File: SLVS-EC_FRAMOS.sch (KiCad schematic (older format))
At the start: 10 parts, among them J21 DF40HC(4.0)-60DS-0.4V(51)

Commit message: Pre-Production Push
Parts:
- added R45, R46: 1K, Resistor_SMD:R_0402_1005Metric, symbol Device:R
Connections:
- net DATA_4_N is gone; now on net SLVS_D1_N: J21.47 (Pin_47)
- net DATA_4_P is gone; now on net SLVS_D1_P: J21.45 (Pin_45)
- net DATA_6_N is gone; now on net SLVS_D0_N: J21.41 (Pin_41)
- net DATA_6_P is gone; now on net SLVS_D0_P: J21.39 (Pin_39)
- net HPC09_P_I2C_SLVS_EC_SCL: now also R46.1
- net HPC12_N_I2C_SLVS_EC_SDA: now also R45.1
- net PL_1V8: now also R45.2, R46.2
- net SLVS_D0_N: now also C261.2; no longer C259.1, J21.59 (Pin_59)
- net SLVS_D0_P: now also C262.2; no longer C260.1, J21.57 (Pin_57)
- net SLVS_D1_N: now also C259.1; no longer C261.2, J21.54 (Pin_54)
- net SLVS_D1_P: now also C260.1; no longer C262.2, J21.52 (Pin_52)
- net GTH_DP0_C2M_SLVS_EC_RX_N renamed GTH_DP1_C2M_SLVS_EC_RX_LANE1_N
- net GTH_DP0_C2M_SLVS_EC_RX_P renamed GTH_DP1_C2M_SLVS_EC_RX_LANE1_P
- net GTH_DP1_C2M_SLVS_EC_RX_N renamed GTH_DP3_C2M_SLVS_EC_RX_LANE0_N
- net GTH_DP1_C2M_SLVS_EC_RX_P renamed GTH_DP3_C2M_SLVS_EC_RX_LANE0_P
- net HPC01_N_GPIO0(XMASTER) renamed HPC01_N_XMASTER
- net HPC06_P_MCLK_0_SLVS renamed HPC10_CC_P_MCLK_0_SLVS
- net HPC10_CC_P_GPIO16_SLAMODE1 renamed HPC_06_P_GPIO16_SLAMODE1
- new net DATA_0_N: J21.59 (Pin_59)
- new net DATA_0_P: J21.57 (Pin_57)
- new net DATA_1_N: J21.54 (Pin_54)
- new net DATA_1_P: J21.52 (Pin_52)
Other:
- note added: "Edit -> Have SCK and XCE and SDA pulled to PL 1V8\nto allow for I2C or SPI communication\nPull down MISO so it does not float"
- note added: "Note, FRAMOS's DATA_#_P/N \nis in respect to SLVS, not SLVS-EC.\nRemember to reference datasheet\n for SLVS-EC pinout"
- moved on the sheet: C254, C255, C256, C257, C259, C260, C261, C262, J21, R217

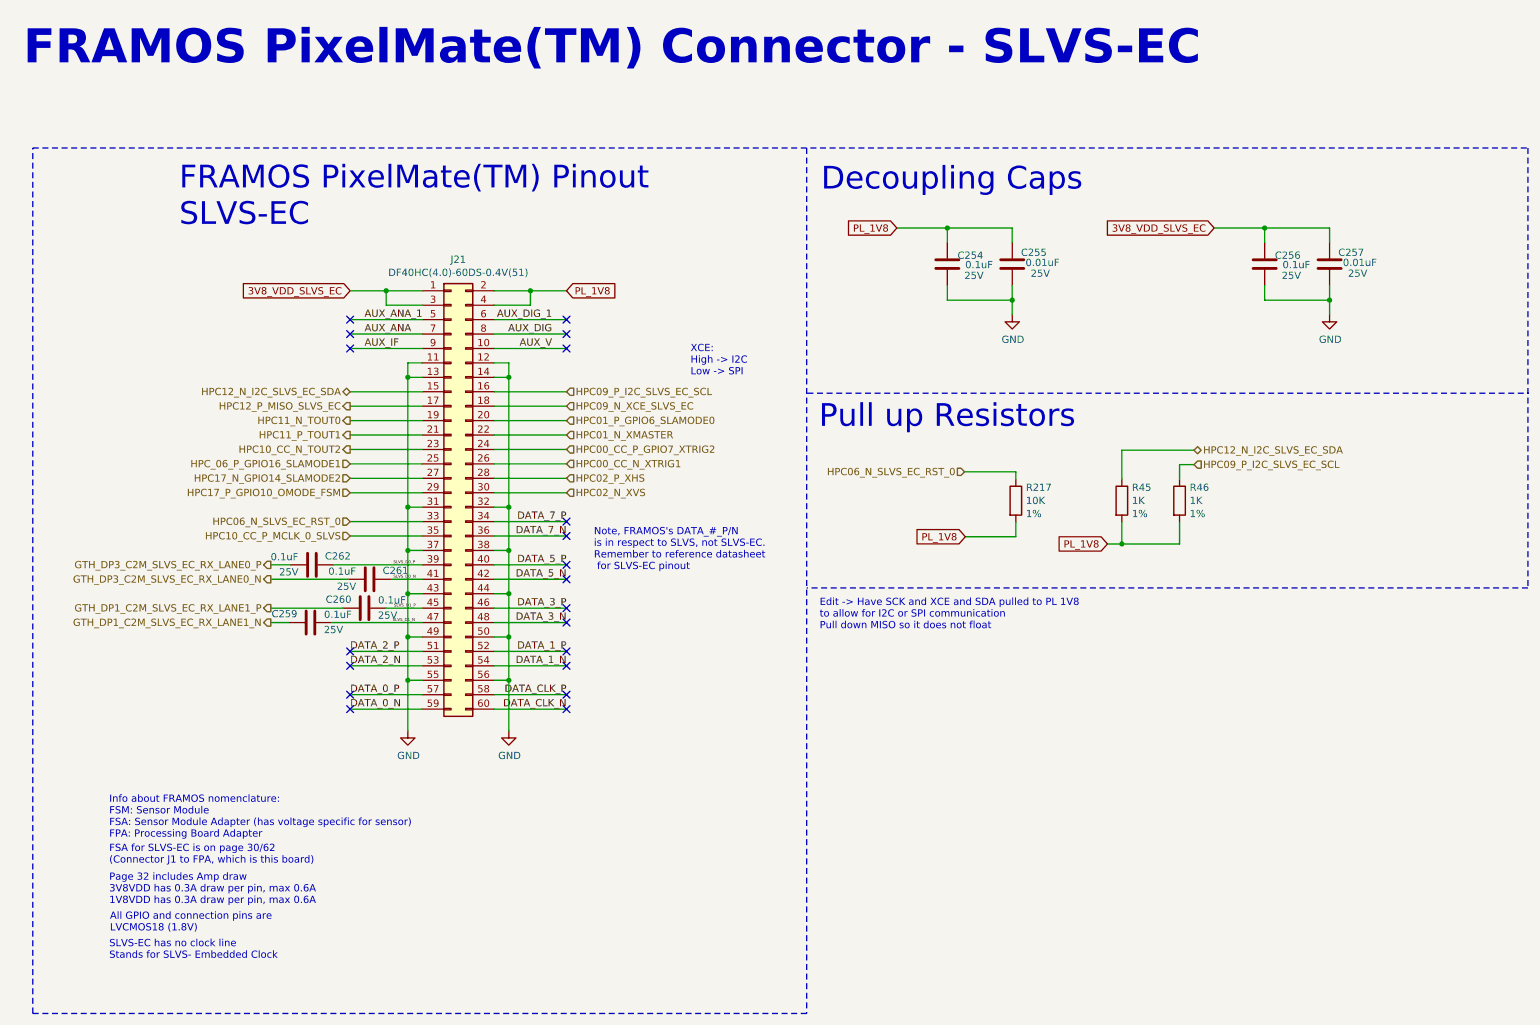
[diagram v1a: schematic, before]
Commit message: Update to Kicad 7
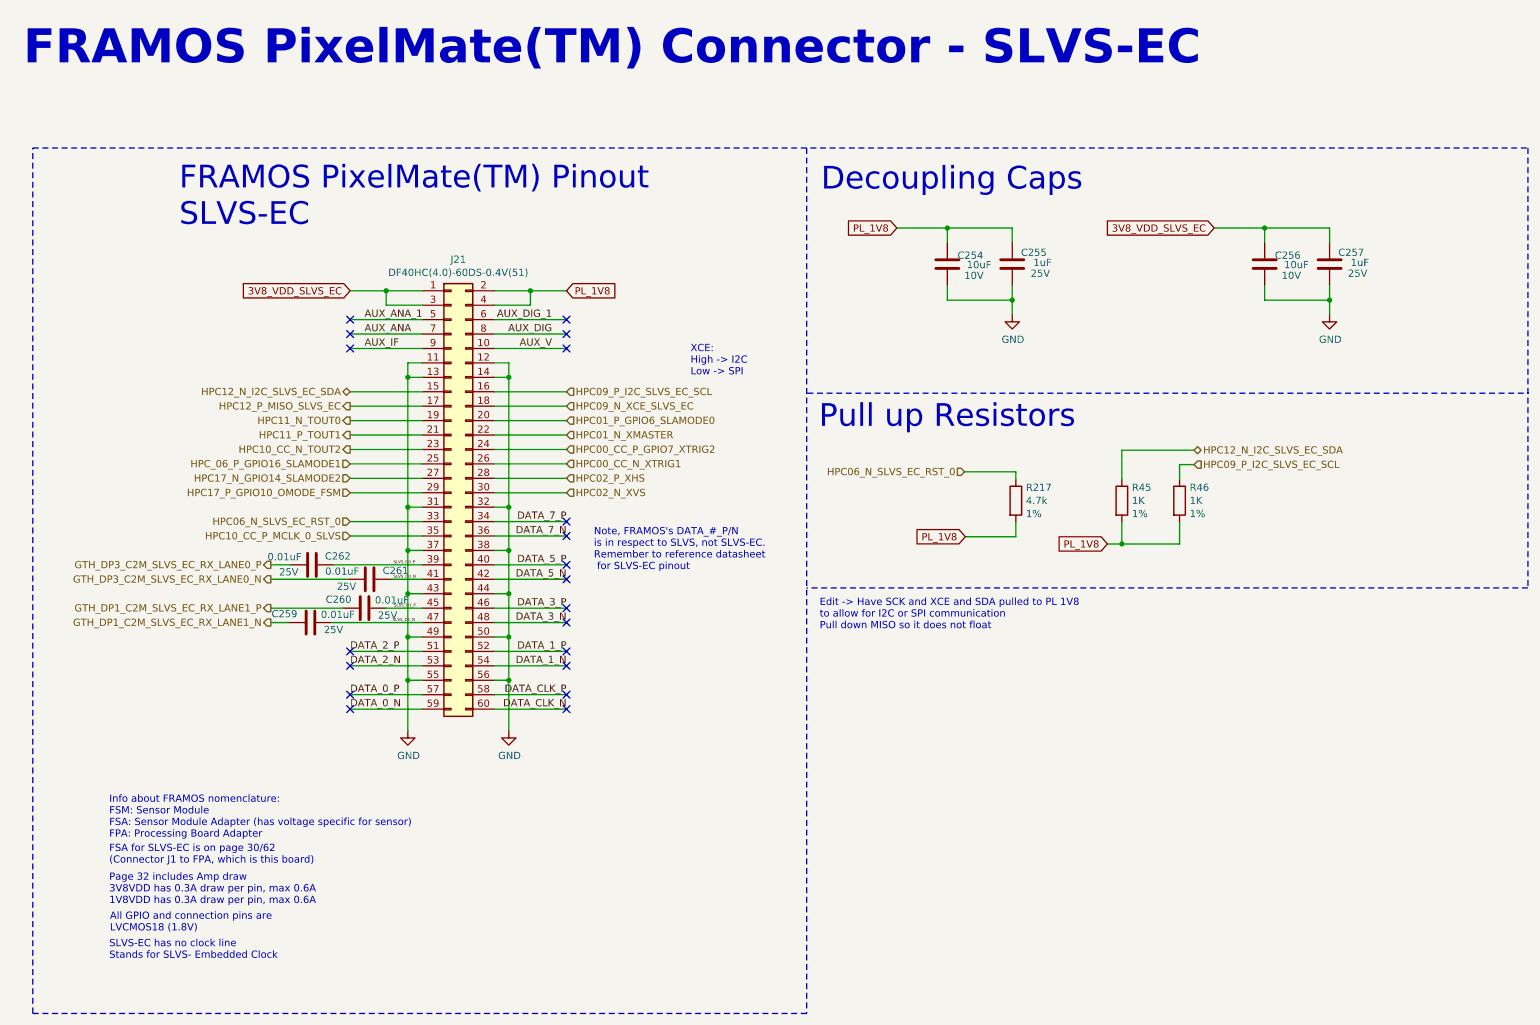
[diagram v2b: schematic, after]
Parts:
- C254, C256: value 0.1uF -> 10uF; PartNumber TMK105BJ104KVHF -> CL05A106MP5NUNC; Tolerance +-10% -> +-20%; URL https://www.digikey.com/en/products/detail/TMK105BJ104KVHF/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 -> https://www.mouser.com/ProductDetail/Samsung-Electro-Mechan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; Voltage 25V -> 10V
- C255, C257: value 0.01uF -> 1uF; PartNumber 04023D103KAT2A -> C1005X5R1E105K050BE; URL (none) -> https://www.digikey.com/en/products/detail/tdk-corporation/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
- C259, C260, C261, C262: value 0.1uF -> 0.01uF; PartNumber TMK105BJ104KVHF -> 04023D103KAT2A; URL https://www.digikey.com/en/products/detail/TMK105BJ104KVHF/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 -> (none)
- R217: value 10K -> 4.7k; PartNumber ERJ-2RKF1002X -> CRCW04024K70FKED; URL https://www.digikey.com/en/products/detail/panasonic-electr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 -> (none)
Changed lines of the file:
@@
 AR Path="/63747F19/62A63FC5" Ref="C254"  Part="1"
 F 0 "C254" H 6830 2250 50  0000 C CNN
-F 1 "0.1uF" H 6770 2315 50  0000 C CNN
+F 1 "10uF" H 6770 2315 50  0000 C CNN
 F 2 "Capacitor_SMD:C_0402_1005Metric" H 7028 2160 50  0001 C CNN
 F 3 "~" H 6990 2310 50  0001 C CNN
-F 4 "TMK105BJ104KVHF" H 6990 2310 50  0001 C CNN "PartNumber"
-F 5 "+-10%" H 6990 2310 50  0001 C CNN "Tolerance"
-F 6 "25V" H 6805 2390 50  0000 C CNN "Voltage"
+F 4 "CL05A106MP5NUNC" H 6990 2310 50  0001 C CNN "PartNumber"
+F 5 "+-20%" H 6990 2310 50  0001 C CNN "Tolerance"
+F 6 "10V" H 6805 2390 50  0000 C CNN "Voltage"
 F 7 "X5R" H 6990 2310 50  0001 C CNN "Temp_Val"
-F 8 "https://www.digikey.com/en/products/detail/TMK105BJ104KVHF/587-3808-1-ND/4811278?itemSeq=375666509" V 6990 2310 50  0001 C CNN "URL"
+F 8 "https://www.mouser.com/ProductDetail/Samsung-Electro-Mechanics/CL05A106MP5NUNC?qs=X6jEic%2FHinA5hRYAnV6SHQ%3D%3D" V 6990 2310 50  0001 C CNN "URL"
 	1    6990 2310
-	-1   0    0    1
-$EndComp
-$Comp
-L Device:C C?
-U 1 1 62A63FCF
-P 7440 2310
-AR Path="/5F71E87D/62A63FCF" Ref="C?"  Part="1"
-AR Path="/5F71E4A6/62A63FCF" Ref="C?"  Part="1"
-AR Path="/6104E394/62A63FCF" Ref="C?"  Part="1"
-AR Path="/637471EA/62A63FCF" Ref="C?"  Part="1"
-AR Path="/61AA736C/62A63FCF" Ref="C?"  Part="1"
-AR Path="/63747F19/62A63FCF" Ref="C255"  Part="1"
-F 0 "C255" H 7290 2230 50  0000 C CNN
-F 1 "0.01uF" H 7230 2300 50  0000 C CNN
-F 2 "Capacitor_SMD:C_0402_1005Metric" H 7478 2160 50  0001 C CNN
-F 3 "~" H 7440 2310 50  0001 C CNN
-F 4 "04023D103KAT2A" H 7440 2310 50  0001 C CNN "PartNumber"
-F 5 "+-10%" H 7440 2310 50  0001 C CNN "Tolerance"
-F 6 "25V" H 7245 2375 50  0000 C CNN "Voltage"
-F 7 "X5R" H 7440 2310 50  0001 C CNN "Temp_Val"
-	1    7440 2310
 	-1   0    0    1
 $EndComp
@@
 AR Path="/63747F19/62A8BEFA" Ref="C256"  Part="1"
 F 0 "C256" H 9030 2250 50  0000 C CNN
-F 1 "0.1uF" H 8970 2315 50  0000 C CNN
+F 1 "10uF" H 8970 2315 50  0000 C CNN
 F 2 "Capacitor_SMD:C_0402_1005Metric" H 9228 2160 50  0001 C CNN
 F 3 "~" H 9190 2310 50  0001 C CNN
-F 4 "TMK105BJ104KVHF" H 9190 2310 50  0001 C CNN "PartNumber"
-F 5 "+-10%" H 9190 2310 50  0001 C CNN "Tolerance"
-F 6 "25V" H 9005 2390 50  0000 C CNN "Voltage"
+F 4 "CL05A106MP5NUNC" H 9190 2310 50  0001 C CNN "PartNumber"
+F 5 "+-20%" H 9190 2310 50  0001 C CNN "Tolerance"
+F 6 "10V" H 9005 2390 50  0000 C CNN "Voltage"
 F 7 "X5R" H 9190 2310 50  0001 C CNN "Temp_Val"
-F 8 "https://www.digikey.com/en/products/detail/TMK105BJ104KVHF/587-3808-1-ND/4811278?itemSeq=375666509" V 9190 2310 50  0001 C CNN "URL"
+F 8 "https://www.mouser.com/ProductDetail/Samsung-Electro-Mechanics/CL05A106MP5NUNC?qs=X6jEic%2FHinA5hRYAnV6SHQ%3D%3D" V 9190 2310 50  0001 C CNN "URL"
 	1    9190 2310
 	-1   0    0    1
@@
 AR Path="/63747F19/62A8BF04" Ref="C257"  Part="1"
 F 0 "C257" H 9490 2230 50  0000 C CNN
-F 1 "0.01uF" H 9430 2300 50  0000 C CNN
+F 1 "1uF" H 9430 2300 50  0000 C CNN
 F 2 "Capacitor_SMD:C_0402_1005Metric" H 9678 2160 50  0001 C CNN
 F 3 "~" H 9640 2310 50  0001 C CNN
-F 4 "04023D103KAT2A" H 9640 2310 50  0001 C CNN "PartNumber"
+F 4 "C1005X5R1E105K050BE" H 9640 2310 50  0001 C CNN "PartNumber"
 F 5 "+-10%" H 9640 2310 50  0001 C CNN "Tolerance"
 F 6 "25V" H 9445 2375 50  0000 C CNN "Voltage"
 F 7 "X5R" H 9640 2310 50  0001 C CNN "Temp_Val"
+F 8 "https://www.digikey.com/en/products/detail/tdk-corporation/C1005X5R1E105K050BE/7907739" H 9640 2310 50  0001 C CNN "URL"
 	1    9640 2310
 	-1   0    0    1
@@
 AR Path="/63747F19/63D18144" Ref="R217"  Part="1"
 F 0 "R217" H 7535 4041 50  0000 L CNN
-F 1 "10K" H 7535 3950 50  0000 L CNN
+F 1 "4.7k" H 7535 3950 50  0000 L CNN
 F 2 "Resistor_SMD:R_0402_1005Metric" V 7395 3950 50  0001 C CNN
 F 3 "~" H 7465 3950 50  0001 C CNN
 F 4 "1%" H 7535 3859 50  0000 L CNN "Tolerance"
 F 5 "1/10W" H 7465 3950 50  0001 C CNN "Power"
-F 6 "ERJ-2RKF1002X" H 7465 3950 50  0001 C CNN "PartNumber"
-F 7 "https://www.digikey.com/en/products/detail/panasonic-electronic-components/ERJ-2RKF1002X/192073" H 7465 3950 50  0001 C CNN "URL"
+F 6 "CRCW04024K70FKED" H 7465 3950 50  0001 C CNN "PartNumber"
 	1    7465 3950
 	1    0    0    -1
@@
 AR Path="/63747F19/62E30CE5" Ref="C260"  Part="1"
 F 0 "C260" V 2890 4515 50  0000 C CNN
-F 1 "0.1uF" V 2895 4885 50  0000 C CNN
+F 1 "0.01uF" V 2895 4885 50  0000 C CNN
 F 2 "Capacitor_SMD:C_0402_1005Metric" H 2988 4545 50  0001 C CNN
 F 3 "~" H 2950 4695 50  0001 C CNN
-F 4 "TMK105BJ104KVHF" H 2950 4695 50  0001 C CNN "PartNumber"
+F 4 "04023D103KAT2A" H 2950 4695 50  0001 C CNN "PartNumber"
 F 5 "+-10%" H 2950 4695 50  0001 C CNN "Tolerance"
 F 6 "25V" V 3000 4855 50  0000 C CNN "Voltage"
 F 7 "X5R" H 2950 4695 50  0001 C CNN "Temp_Val"
-F 8 "https://www.digikey.com/en/products/detail/TMK105BJ104KVHF/587-3808-1-ND/4811278?itemSeq=375666509" V 2950 4695 50  0001 C CNN "URL"
 	1    2950 4695
 	0    1    1    0
@@
 AR Path="/63747F19/62E402ED" Ref="C259"  Part="1"
 F 0 "C259" V 2515 4615 50  0000 C CNN
-F 1 "0.1uF" V 2520 4985 50  0000 C CNN
+F 1 "0.01uF" V 2520 4985 50  0000 C CNN
 F 2 "Capacitor_SMD:C_0402_1005Metric" H 2613 4645 50  0001 C CNN
 F 3 "~" H 2575 4795 50  0001 C CNN
-F 4 "TMK105BJ104KVHF" H 2575 4795 50  0001 C CNN "PartNumber"
+F 4 "04023D103KAT2A" H 2575 4795 50  0001 C CNN "PartNumber"
 F 5 "+-10%" H 2575 4795 50  0001 C CNN "Tolerance"
 F 6 "25V" V 2625 4955 50  0000 C CNN "Voltage"
 F 7 "X5R" H 2575 4795 50  0001 C CNN "Temp_Val"
-F 8 "https://www.digikey.com/en/products/detail/TMK105BJ104KVHF/587-3808-1-ND/4811278?itemSeq=375666509" V 2575 4795 50  0001 C CNN "URL"
 	1    2575 4795
 	0    1    1    0
@@
 AR Path="/63747F19/62E6700A" Ref="C261"  Part="1"
 F 0 "C261" V 2925 4315 50  0000 C CNN
-F 1 "0.1uF" V 2930 4685 50  0000 C CNN
+F 1 "0.01uF" V 2930 4685 50  0000 C CNN
 F 2 "Capacitor_SMD:C_0402_1005Metric" H 3023 4345 50  0001 C CNN
 F 3 "~" H 2985 4495 50  0001 C CNN
-F 4 "TMK105BJ104KVHF" H 2985 4495 50  0001 C CNN "PartNumber"
+F 4 "04023D103KAT2A" H 2985 4495 50  0001 C CNN "PartNumber"
 F 5 "+-10%" H 2985 4495 50  0001 C CNN "Tolerance"
 F 6 "25V" V 3035 4655 50  0000 C CNN "Voltage"
 F 7 "X5R" H 2985 4495 50  0001 C CNN "Temp_Val"
-F 8 "https://www.digikey.com/en/products/detail/TMK105BJ104KVHF/587-3808-1-ND/4811278?itemSeq=375666509" V 2985 4495 50  0001 C CNN "URL"
 	1    2985 4495
 	0    -1   1    0
@@
 AR Path="/63747F19/62E7792E" Ref="C262"  Part="1"
 F 0 "C262" V 2525 4215 50  0000 C CNN
-F 1 "0.1uF" V 2530 4585 50  0000 C CNN
+F 1 "0.01uF" V 2530 4585 50  0000 C CNN
 F 2 "Capacitor_SMD:C_0402_1005Metric" H 2623 4245 50  0001 C CNN
 F 3 "~" H 2585 4395 50  0001 C CNN
-F 4 "TMK105BJ104KVHF" H 2585 4395 50  0001 C CNN "PartNumber"
+F 4 "04023D103KAT2A" H 2585 4395 50  0001 C CNN "PartNumber"
 F 5 "+-10%" H 2585 4395 50  0001 C CNN "Tolerance"
 F 6 "25V" V 2635 4555 50  0000 C CNN "Voltage"
 F 7 "X5R" H 2585 4395 50  0001 C CNN "Temp_Val"
-F 8 "https://www.digikey.com/en/products/detail/TMK105BJ104KVHF/587-3808-1-ND/4811278?itemSeq=375666509" V 2585 4395 50  0001 C CNN "URL"
 	1    2585 4395
 	0    -1   1    0
@@
 Wire Wire Line
 	8200 3600 8200 3800
+$Comp
+L Device:C C?
+U 1 1 63B954A9
+P 7440 2310
+AR Path="/5F71E87D/63B954A9" Ref="C?"  Part="1"
+AR Path="/5F71E4A6/63B954A9" Ref="C?"  Part="1"
+AR Path="/6104E394/63B954A9" Ref="C?"  Part="1"
+AR Path="/637471EA/63B954A9" Ref="C?"  Part="1"
+AR Path="/61AA736C/63B954A9" Ref="C?"  Part="1"
+AR Path="/63747F19/63B954A9" Ref="C255"  Part="1"
+F 0 "C255" H 7290 2230 50  0000 C CNN
+F 1 "1uF" H 7230 2300 50  0000 C CNN
+F 2 "Capacitor_SMD:C_0402_1005Metric" H 7478 2160 50  0001 C CNN
+F 3 "~" H 7440 2310 50  0001 C CNN
+F 4 "C1005X5R1E105K050BE" H 7440 2310 50  0001 C CNN "PartNumber"
+F 5 "+-10%" H 7440 2310 50  0001 C CNN "Tolerance"
+F 6 "25V" H 7245 2375 50  0000 C CNN "Voltage"
+F 7 "X5R" H 7440 2310 50  0001 C CNN "Temp_Val"
+F 8 "https://www.digikey.com/en/products/detail/tdk-corporation/C1005X5R1E105K050BE/7907739" H 7440 2310 50  0001 C CNN "URL"
+	1    7440 2310
+	-1   0    0    1
+$EndComp
 $EndSCHEMATC
